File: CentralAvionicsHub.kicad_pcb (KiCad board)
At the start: 2 copper layers, 106.6 x 87.9 mm, 18 parts, among them J1 GPS/ARINC, J2 MFD, J3 PFD, J4 NavCom, J5 Airframe, J6 GND1, J7 GND2, J8 Power_In, J9 Switches_Indicators

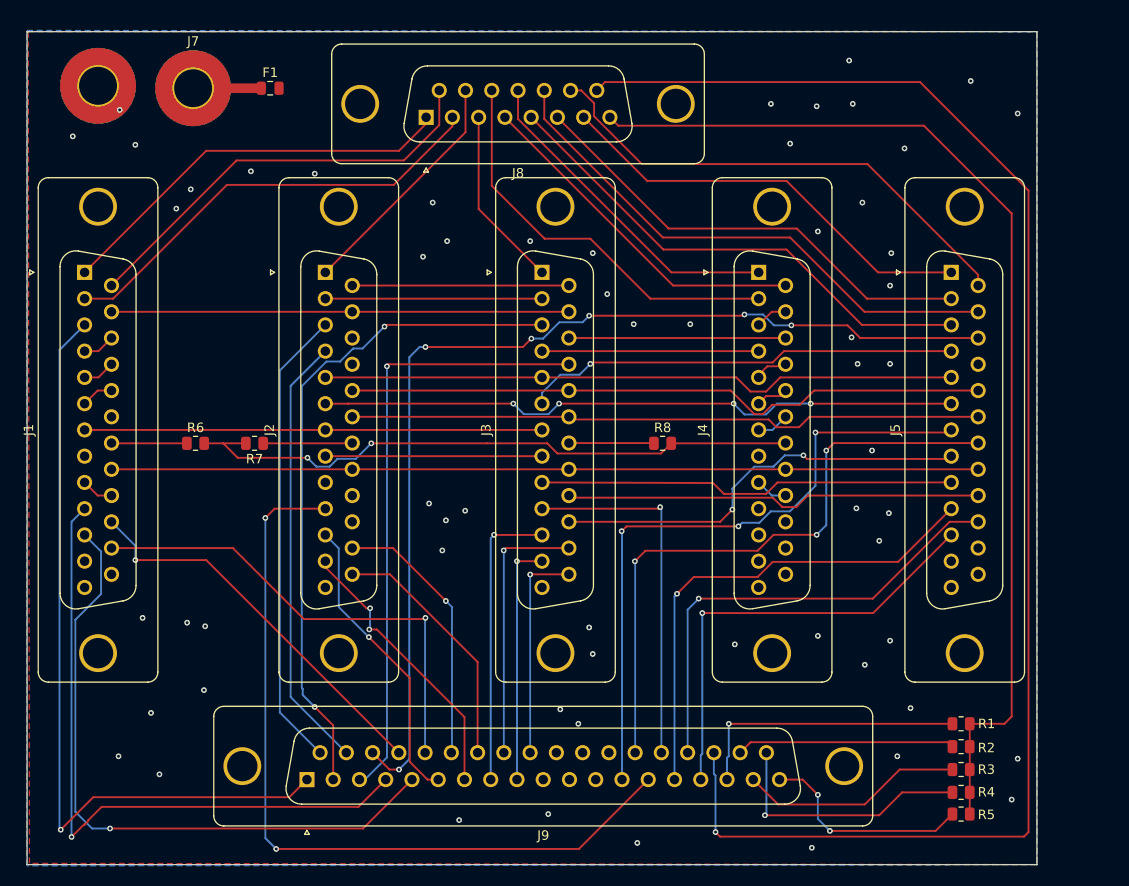
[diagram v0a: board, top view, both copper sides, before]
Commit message: Added mounting holes, aligned components, began power layout with properly sized traces.
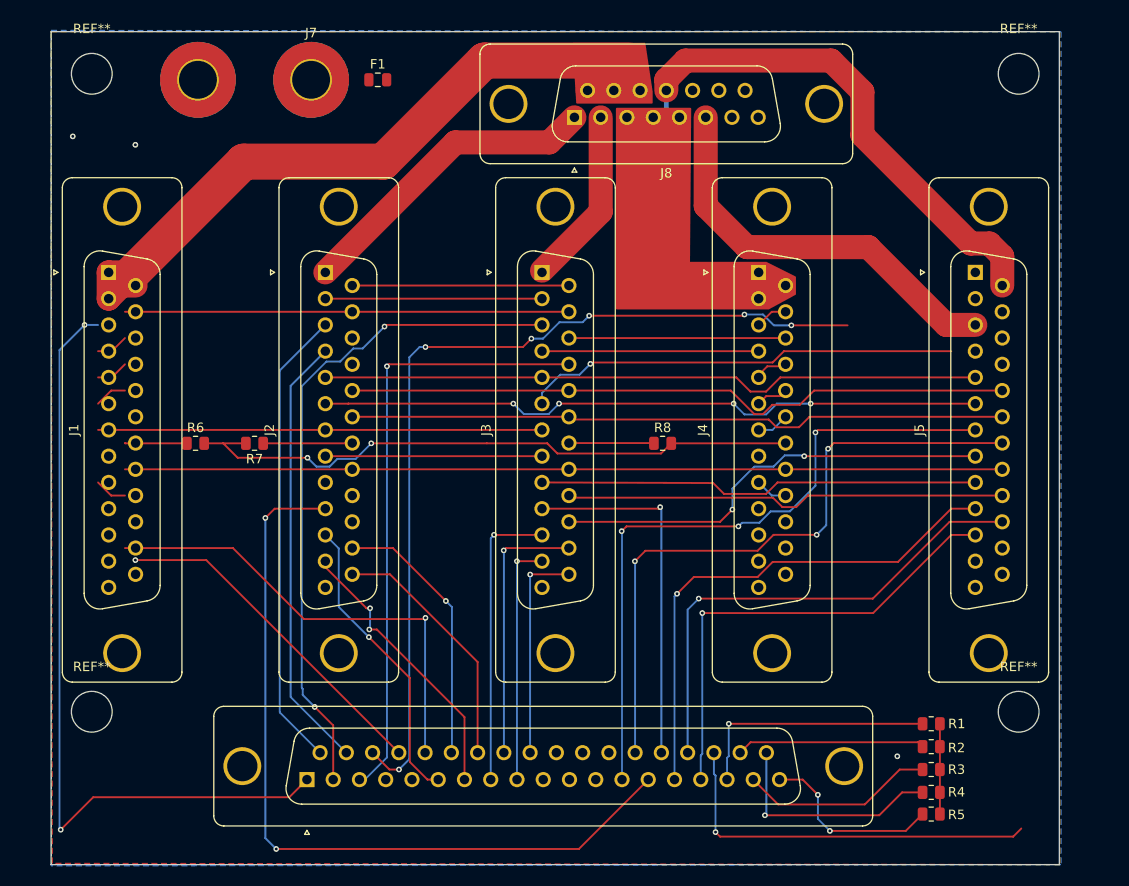
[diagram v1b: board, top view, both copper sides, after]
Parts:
- added REF**: MountingHole_4.3mm_M4_ISO7380, MountingHole:MountingHole_4.3mm_M4_ISO7380, F.Cu at (100.9, 65.4)
- added REF**: MountingHole_4.3mm_M4_ISO7380, MountingHole:MountingHole_4.3mm_M4_ISO7380, F.Cu at (198.7, 65.4)
- added REF**: MountingHole_4.3mm_M4_ISO7380, MountingHole:MountingHole_4.3mm_M4_ISO7380, F.Cu at (100.9, 132.7)
- added REF**: MountingHole_4.3mm_M4_ISO7380, MountingHole:MountingHole_4.3mm_M4_ISO7380, F.Cu at (198.7, 132.7)
- moved J8 15.6 mm to (151.9, 70.0)
- moved J7 12.5 mm to (124.1, 66.0)
- moved F1 11.4 mm to (131.1, 66.0)
- moved J6 10.6 mm to (112.1, 66.0)
- moved R1 3.15 mm to (189.5, 134.0)
- moved R2 3.15 mm to (189.5, 136.4)
- moved R3 3.15 mm to (189.5, 138.8)
- moved R4 3.15 mm to (189.5, 141.2)
- moved R5 3.15 mm to (189.5, 143.5)
- moved J1 2.54 mm to (102.7, 86.4)
- moved J5 2.54 mm to (194.2, 86.4)
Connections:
- J1 pad 1: Net-(J1-Pad1) -> Net-(J1-P14)
- J1 pad 2: Net-(J1-Pad2) -> Net-(J1-P14)
- J2 pad 1: Net-(J8-P10) -> Net-(J2-Pad1)
- J4 pad 1: Net-(J8-P12) -> Net-(J4-P14)
- J4 pad 2: Net-(J8-P111) -> Net-(J4-P14)
- J5 pad 1: Net-(J5-Pad1) -> unconnected-(J5-Pad1)
- J5 pad 15: Net-(J5-P15) -> unconnected-(J5-P15-Pad15)
- J5 pad 2: Net-(J5-Pad2) -> unconnected-(J5-Pad2)
- J8 pad 1: Net-(J1-Pad1) -> Net-(J2-Pad1)
- J8 pad 10: Net-(J8-P10) -> Net-(J1-P14)
- J8 pad 11: Net-(J8-P111) -> Net-(J1-P14)
- J8 pad 12: Net-(J8-P12) -> Net-(J5-P14)
- J8 pad 13: Net-(J5-P15) -> unconnected-(J8-P13-Pad13)
- J8 pad 14: Net-(J5-P14) -> unconnected-(J8-P14-Pad14)
- J8 pad 15: Net-(J8-P15) -> unconnected-(J8-P15-Pad15)
- J8 pad 2: Net-(J1-Pad2) -> Net-(J3-Pad1)
- J8 pad 3: Net-(J3-Pad1) -> Net-(J4-P14)
- J8 pad 5: Net-(J5-Pad3) -> Net-(J4-P14)
- J8 pad 6: Net-(J5-Pad2) -> Net-(J5-Pad3)
- J8 pad 7: Net-(J5-Pad1) -> unconnected-(J8-Pad7)
- J8 pad 8: Net-(J8-Pad8) -> unconnected-(J8-Pad8)
- J9 pad 35: Net-(J8-P15) -> unconnected-(J9-Pad35)
- R1 pad 2: Net-(J8-Pad8) -> Net-(R1-Pad2)
- R2 pad 2: Net-(J8-Pad8) -> Net-(R1-Pad2)
- R3 pad 2: Net-(J8-Pad8) -> Net-(R1-Pad2)
- R4 pad 2: Net-(J8-Pad8) -> Net-(R1-Pad2)
- R5 pad 2: Net-(J8-Pad8) -> Net-(R1-Pad2)
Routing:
- net Net-(J8-P15): track 160.2 -> 0.00 mm, vias 1 -> 0
- net Net-(J8-Pad8): track 113.9 -> 0.00 mm
- net /GPS_AUX1: track 70.9 -> 0.00 mm, vias 1 -> 0
- net /GPS_AUX3: track 69.4 -> 0.00 mm, vias 1 -> 0
- net Net-(J5-P15): track 57.2 -> 0.00 mm
- net Net-(J5-Pad2): track 49.5 -> 0.00 mm
- net Net-(J1-Pad2): track 47.3 -> 0.00 mm
- net Net-(J5-Pad1): track 45.6 -> 0.00 mm
- net Net-(J1-Pad1): track 43.2 -> 0.00 mm
- net Net-(J8-P111): track 43.2 -> 0.00 mm
- net unconnected-(J9-Pad35): track 0.00 -> 41.3 mm, vias 0 -> 1
- net Net-(J4-P14): track 37.0 -> 0.00 mm
- net Net-(J8-P12): track 35.1 -> 0.00 mm
- net Net-(J2-Pad1): track 0.00 -> 33.1 mm
- net Net-(J1-P14): track 45.2 -> 75.9 mm
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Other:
- board size 106.6 x 87.9 mm -> 106.4 x 87.9 mm

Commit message: Power routing mostly complete. Rearranged pinout on power_in connector to support better routing. Broke a number of other traces in the process, will correct later.
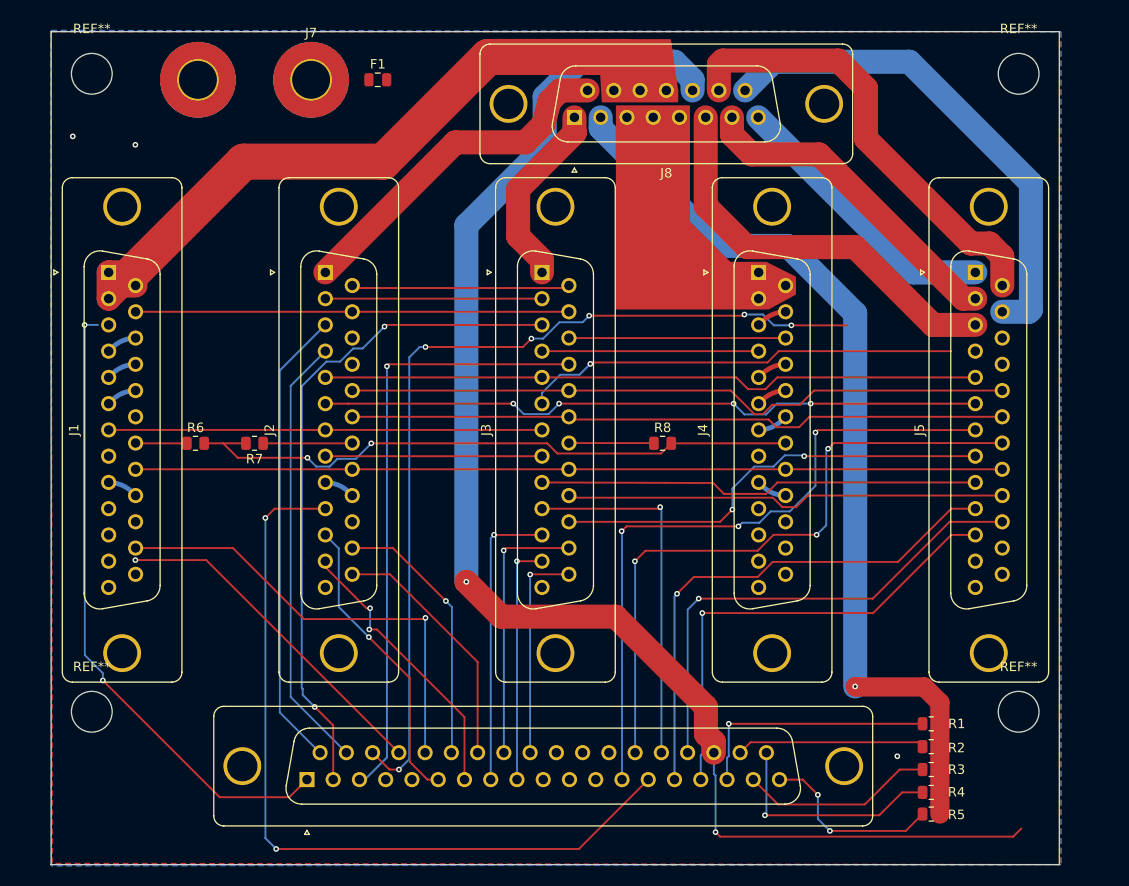
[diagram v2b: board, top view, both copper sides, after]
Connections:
- J2 pad 1: Net-(J2-Pad1) -> Net-(J8-P9)
- J5 pad 1: unconnected-(J5-Pad1) -> Net-(J5-Pad1)
- J5 pad 15: unconnected-(J5-P15-Pad15) -> Net-(J5-P15)
- J5 pad 2: unconnected-(J5-Pad2) -> Net-(J5-Pad2)
- J8 pad 1: Net-(J2-Pad1) -> Net-(J3-Pad1)
- J8 pad 12: Net-(J5-P14) -> Net-(J1-P14)
- J8 pad 13: unconnected-(J8-P13-Pad13) -> Net-(J8-P13)
- J8 pad 14: unconnected-(J8-P14-Pad14) -> Net-(J5-P14)
- J8 pad 15: unconnected-(J8-P15-Pad15) -> Net-(J5-P15)
- J8 pad 2: Net-(J3-Pad1) -> Net-(J8-Pad2)
- J8 pad 7: unconnected-(J8-Pad7) -> Net-(J5-Pad2)
- J8 pad 8: unconnected-(J8-Pad8) -> Net-(J5-Pad1)
- J8 pad 9: Net-(J1-P14) -> Net-(J8-P9)
- J9 pad 35: unconnected-(J9-Pad35) -> Net-(J8-P13)
- R1 pad 2: Net-(R1-Pad2) -> Net-(J8-Pad2)
- R2 pad 2: Net-(R1-Pad2) -> Net-(J8-Pad2)
- R3 pad 2: Net-(R1-Pad2) -> Net-(J8-Pad2)
- R4 pad 2: Net-(R1-Pad2) -> Net-(J8-Pad2)
- R5 pad 2: Net-(R1-Pad2) -> Net-(J8-Pad2)
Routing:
- net Net-(J8-P13): track 0.00 -> 150.8 mm, vias 0 -> 2
- net Net-(J8-Pad2): track 0.00 -> 106.4 mm, vias 0 -> 1
- net Net-(J5-P15): track 0.00 -> 53.2 mm
- net unconnected-(J9-Pad35): track 41.3 -> 0.00 mm, vias 1 -> 0
- net Net-(J8-P9): track 0.00 -> 36.5 mm
- net Net-(J5-Pad2): track 0.00 -> 34.7 mm
- net Net-(J2-Pad1): track 33.1 -> 0.00 mm
- net Net-(J5-Pad1): track 0.00 -> 29.7 mm
- net /ARINC_Serial_RX: track 84.0 -> 67.1 mm
- net Net-(R1-Pad2): track 9.52 -> 0.00 mm
- net Net-(J5-P14): track 57.1 -> 47.6 mm
- net Net-(J1-P14): track 75.9 -> 70.6 mm
- net Net-(J2-P22): track 0.00 -> 3.24 mm
- net Net-(J3-Pad1): track 18.7 -> 19.9 mm
- net /Lighting_Bus: track 92.6 -> 91.4 mm
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
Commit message: Removed Curved Traces
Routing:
- net Net-(J4-P22): track 3.24 -> 0.50 mm
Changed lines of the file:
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@@
+	(segment
+		(start 102.72014 94.67)
+		(end 105.56014 93.285)
+		(width 0.508)
+		(layer "F.Cu")
+		(net 4)
+	)
 	(segment
 		(start 102.72014 94.67)
@@
 		(net 4)
 	)
-	(arc
-		(start 103.0763 94.31384)
-		(mid 104.215895 93.552387)
-		(end 105.56014 93.285)
-		(width 0.508)
-		(layer "B.Cu")
-		(net 4)
+	(segment
+		(start 102.72014 97.44)
+		(end 105.56014 96.055)
+		(width 0.508)
+		(layer "F.Cu")
+		(net 5)
 	)
 	(segment
@@
 		(net 5)
 	)
-	(arc
-		(start 103.0763 97.08384)
-		(mid 104.215895 96.322387)
-		(end 105.56014 96.055)
-		(width 0.508)
-		(layer "B.Cu")
-		(net 5)
+	(segment
+		(start 102.72014 108.52)
+		(end 105.56014 109.905)
+		(width 0.508)
+		(layer "F.Cu")
+		(net 6)
 	)
 	(segment
@@
 		(net 6)
 	)
-	(arc
-		(start 102.72014 108.52)
-		(mid 104.064385 108.787387)
-		(end 105.203981 109.54884)
-		(width 0.508)
-		(layer "B.Cu")
-		(net 6)
-	)
 	(segment
 		(start 123.317 122.936)
@@
 	(segment
 		(start 102.72014 100.21)
+		(end 105.56014 98.825)
+		(width 0.508)
+		(layer "F.Cu")
+		(net 10)
+	)
+	(segment
+		(start 102.72014 100.21)
 		(end 103.0763 99.85384)
-		(width 0.508)
-		(layer "B.Cu")
-		(net 10)
-	)
-	(arc
-		(start 103.0763 99.85384)
-		(mid 104.215895 99.092387)
-		(end 105.56014 98.825)
 		(width 0.508)
 		(layer "B.Cu")
@@
 	)
 	(segment
+		(start 125.58 108.52)
+		(end 128.42 109.905)
+		(width 0.508)
+		(layer "F.Cu")
+		(net 19)
+	)
+	(segment
 		(start 128.063841 109.54884)
 		(end 128.42 109.905)
-		(width 0.508)
-		(layer "B.Cu")
-		(net 19)
-	)
-	(arc
-		(start 125.58 108.52)
-		(mid 126.924245 108.787387)
-		(end 128.063841 109.54884)
 		(width 0.508)
 		(layer "B.Cu")
@@
 	(segment
 		(start 171.3 100.21)
+		(end 174.14 98.825)
+		(width 0.508)
+		(layer "F.Cu")
+		(net 49)
+	)
+	(segment
+		(start 171.3 100.21)
 		(end 171.65616 99.85384)
-		(width 0.508)
-		(layer "F.Cu")
-		(net 49)
-	)
-	(arc
-		(start 171.65616 99.85384)
-		(mid 172.795755 99.092387)
-		(end 174.14 98.825)
 		(width 0.508)
 		(layer "F.Cu")
@@
 		(net 50)
 	)
-	(arc
-		(start 174.14 109.905)
-		(mid 172.795755 109.637613)
-		(end 171.656159 108.87616)
-		(width 0.508)
-		(layer "B.Cu")
-		(net 50)
-	)
 	(segment
 		(start 171.3 97.44)
@@
 		(net 51)
 	)
-	(arc
-		(start 171.65616 97.08384)
-		(mid 172.795755 96.322387)
+	(segment
+		(start 171.3 97.44)
 		(end 174.14 96.055)
 		(width 0.508)
 		(layer "F.Cu")
 		(net 51)
+	)
+	(segment
+		(start 171.3 102.98)
+		(end 174.14 101.595)
+		(width 0.508)
+		(layer "B.Cu")
+		(net 52)
 	)
 	(segment
@@
 		(net 52)
 	)
-	(arc
-		(start 171.3 102.98)
-		(mid 172.644245 102.712613)
-		(end 173.783841 101.95116)
-		(width 0.508)
-		(layer "B.Cu")
-		(net 52)
-	)
 	(segment
 		(start 142.621 104.394)
@@
 		(net 54)
 	)
-	(arc
-		(start 171.65616 91.54384)
-		(mid 172.795755 90.782387)
+	(segment
+		(start 171.3 91.9)
 		(end 174.14 90.515)
 		(width 0.508)

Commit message: Trace cleanup
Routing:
- net Net-(J9-Pad17): track 26.4 -> 25.5 mm, vias 1 -> 2
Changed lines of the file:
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@@
 	(gr_poly
 		(pts
-			(xy 156.337 68.834) (xy 156.337 90.17) (xy 172.339 90.17) (xy 175.133 88.646) (xy 175.133 86.868)
-			(xy 172.085 85.344) (xy 168.275 85.344) (xy 163.957 81.026) (xy 163.957 68.834)
+			(xy 156.591 69.342) (xy 156.591 82.423) (xy 163.576 89.662) (xy 172.339 89.662) (xy 174.752 88.265)
+			(xy 174.752 86.995) (xy 172.212 85.852) (xy 169.037 85.852) (xy 163.449 80.264) (xy 163.449 69.342)
 		)
 		(stroke
-			(width 0.2)
+			(width 1.016)
 			(type solid)
 		)
@@
 	(gr_poly
 		(pts
-			(xy 162.716019 67.183) (xy 161.954019 61.849) (xy 154.461019 61.849) (xy 154.842019 68.326) (xy 162.716019 68.326)
+			(xy 162.722932 67.183) (xy 161.960932 62.23) (xy 154.975932 62.23) (xy 155.448 67.945) (xy 162.722932 67.945)
 		)
 		(stroke
-			(width 0.2)
+			(width 1.016)
 			(type solid)
 		)
@@
 	)
 	(segment
-		(start 131.699 74.676)
-		(end 142.748 63.627)
-		(width 3.81)
-		(layer "F.Cu")
-		(net 15)
-	)
-	(segment
-		(start 116.967 74.676)
-		(end 131.699 74.676)
+		(start 142.748 63.627)
+		(end 157.226 63.627)
 		(width 3.81)
 		(layer "F.Cu")
@@
 	)
 	(segment
-		(start 142.748 63.627)
-		(end 157.226 63.627)
-		(width 3.81)
-		(layer "F.Cu")
-		(net 15)
-	)
-	(segment
 		(start 104.10514 87.745)
 		(end 105.56014 87.745)
@@
 	)
 	(segment
+		(start 117.348 74.295)
+		(end 132.08 74.295)
+		(width 3.81)
+		(layer "F.Cu")
+		(net 15)
+	)
+	(segment
+		(start 132.08 74.295)
+		(end 142.748 63.627)
+		(width 3.81)
+		(layer "F.Cu")
+		(net 15)
+	)
+	(segment
 		(start 105.283 86.36)
-		(end 116.967 74.676)
+		(end 117.348 74.295)
 		(width 3.81)
 		(layer "F.Cu")
@@
 	)
 	(segment
-		(start 188.595 133.985)
-		(end 168.148 133.985)
+		(start 170.307 138.176)
+		(end 168.61 139.873)
+		(width 0.2032)
+		(layer "F.Cu")
+		(net 67)
+	)
+	(segment
+		(start 170.688 133.985)
+		(end 188.595 133.985)
 		(width 0.2)
 		(layer "F.Cu")
 		(net 67)
 	)
+	(segment
+		(start 168.61 139.873)
+		(end 167.961 139.873)
+		(width 0.2032)
+		(layer "F.Cu")
+		(net 67)
+	)
+	(segment
+		(start 170.688 138.176)
+		(end 170.307 138.176)
+		(width 0.2032)
+		(layer "F.Cu")
+		(net 67)
+	)
 	(via
-		(at 168.148 133.985)
+		(at 170.688 138.176)
 		(size 0.6)
 		(drill 0.3)
@@
 		(net 67)
 	)
-	(segment
-		(start 168.148 137.39205)
-		(end 167.961 137.57905)
-		(width 0.2)
-		(layer "B.Cu")
-		(net 67)
-	)
-	(segment
-		(start 168.148 133.985)
-		(end 168.148 137.39205)
-		(width 0.2)
-		(layer "B.Cu")
+	(via
+		(at 170.688 133.985)
+		(size 0.6)
+		(drill 0.3)
+		(layers "F.Cu" "B.Cu")
 		(net 67)
 	)
 	(segment
-		(start 167.961 137.57905)
-		(end 167.961 139.873)
-		(width 0.2)
+		(start 170.688 133.985)
+		(end 170.688 138.176)
+		(width 0.2032)
 		(layer "B.Cu")
 		(net 67)
@@
 	)
 	(segment
+		(start 149.225 68.760641)
+		(end 149.121 68.864641)
+		(width 2.54)
+		(layer "F.Cu")
+		(net 69)
+	)
+	(segment
+		(start 149.591 67.729)
+		(end 149.591 67.942916)
+		(width 2.54)
+		(layer "F.Cu")
+		(net 69)
+	)
+	(segment
+		(start 149.121 68.864641)
+		(end 149.121 69.7)
+		(width 2.54)
+		(layer "F.Cu")
+		(net 69)
+	)
+	(segment
 		(start 149.225 68.326)
-		(end 148.59 70.739)
+		(end 149.225 68.760641)
 		(width 2.54)
 		(layer "F.Cu")
@@
 	)
 	(segment
-		(start 146.685 72.644)
-		(end 139.296 72.644)
+		(start 149.795376 67.729)
+		(end 149.591 67.729)
 		(width 2.54)
 		(layer "F.Cu")
@@
 	(segment
 		(start 150.339 67.16)
-		(end 149.225 68.326)
+		(end 149.795376 67.729)
 		(width 2.54)
 		(layer "F.Cu")
@@
 	)
 	(segment
-		(start 148.59 70.739)
-		(end 146.685 72.644)
+		(start 135.128 83.693)
+		(end 128.247 83.693)
 		(width 2.54)
 		(layer "F.Cu")
@@
 	)
 	(segment
-		(start 139.296 72.644)
+		(start 128.247 83.693)
 		(end 125.58 86.36)
 		(width 2.54)
@@
 	)
 	(segment
+		(start 149.591 67.942916)
+		(end 149.225 68.326)
+		(width 2.54)
+		(layer "F.Cu")
+		(net 69)
+	)
+	(segment
+		(start 149.121 69.7)
+		(end 135.128 83.693)
+		(width 2.54)
+		(layer "F.Cu")
+		(net 69)
+	)
+	(segment
 		(start 181.53 130.095)
 		(end 188.769 130.095)
@@
 	)
 	(segment
-		(start 166.576 135.90163)
-		(end 166.576 137.033)
+		(start 140.462 118.999)
+		(end 144.145 122.682)
 		(width 2.54)
 		(layer "F.Cu")
@@
 	)
 	(segment
-		(start 165.735 135.06063)
-		(end 166.576 135.90163)
-		(width 2.54)
-		(layer "F.Cu")
-		(net 71)
-	)
-	(segment
 		(start 144.145 122.682)
 		(end 156.21 122.682)
@@
 	(segment
 		(start 156.21 122.682)
-		(end 165.735 132.207)
+		(end 166.576 133.048)
 		(width 2.54)
 		(layer "F.Cu")
@@
 	)
 	(segment
-		(start 165.735 132.207)
-		(end 165.735 135.06063)
-		(width 2.54)
-		(layer "F.Cu")
-		(net 71)
-	)
-	(segment
-		(start 140.462 118.999)
-		(end 144.145 122.682)
+		(start 166.576 133.048)
+		(end 166.576 137.033)
 		(width 2.54)
 		(layer "F.Cu")
@@
 	)
 	(segment
-		(start 177.673 73.914)
-		(end 170.561 73.914)
+		(start 171.323 74.676)
+		(end 168.482 71.835)
 		(width 2.54)
 		(layer "F.Cu")
@@
 	)
 	(segment
-		(start 168.482 71.835)
-		(end 168.482 70)
+		(start 178.435 74.676)
+		(end 171.323 74.676)
 		(width 2.54)
 		(layer "F.Cu")
@@
 	)
 	(segment
-		(start 170.561 73.914)
-		(end 168.482 71.835)
+		(start 168.482 71.835)
+		(end 168.482 70)
 		(width 2.54)
 		(layer "F.Cu")
@@
 	(segment
 		(start 192.889 89.13)
-		(end 177.673 73.914)
+		(end 178.435 74.676)
 		(width 2.54)
 		(layer "F.Cu")
